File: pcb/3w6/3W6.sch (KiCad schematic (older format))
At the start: 115 parts, among them J1 USB_C Main, J2 USB_C I2C_L, J3 USB_C I2C_R, SW1 SW_Push, SW10 SW_Push, SW11 SW_Push, SW12 SW_Push, SW13 SW_Push, SW14 SW_Push, SW15 SW_Push, SW16 SW_Push, SW17 SW_Push, SW18 SW_Push, SW19 SW_Push, SW2 SW_Push, SW20 SW_Push, SW21 SW_Push, SW22 SW_Push, SW23 SW_Push, SW24 SW_Push, SW25 SW_Push, SW26 SW_Push, SW27 SW_Push, SW28 SW_Push, SW29 SW_Push, SW3 SW_Push, SW30 SW_Push, SW31 SW_Push, SW32 SW_Push, SW33 SW_Push, SW34 SW_Push, SW35 SW_Push, SW36 SW_Push, SW37 SW_Push, SW4 SW_Push, SW5 SW_Push, SW6 SW_Push, SW7 SW_Push, SW8 SW_Push, SW9 SW_Push, U2 TCA9555RTWR, U3 ATmega32U4-MU, Y1 16MHZ

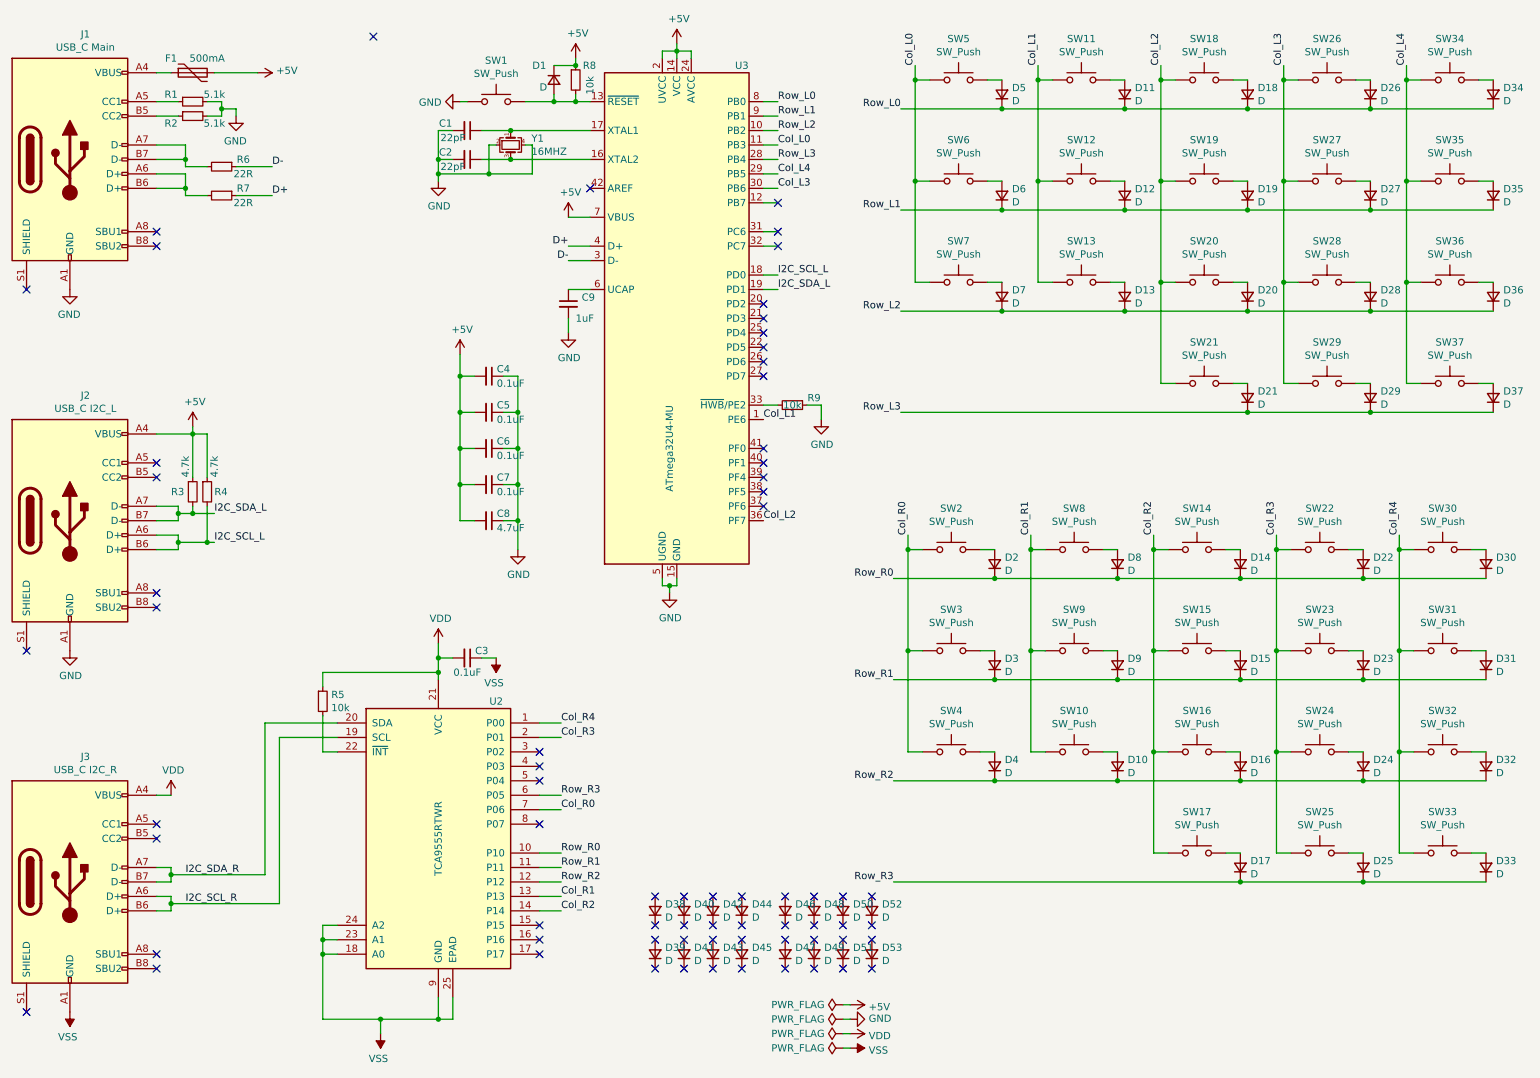
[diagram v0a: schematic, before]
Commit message: add: middle plate chg: rerouting whole board, to eliminate traces under middle plate chg: repositioning components to get a higher clearance in case an aluminium or steel middle plate is used.
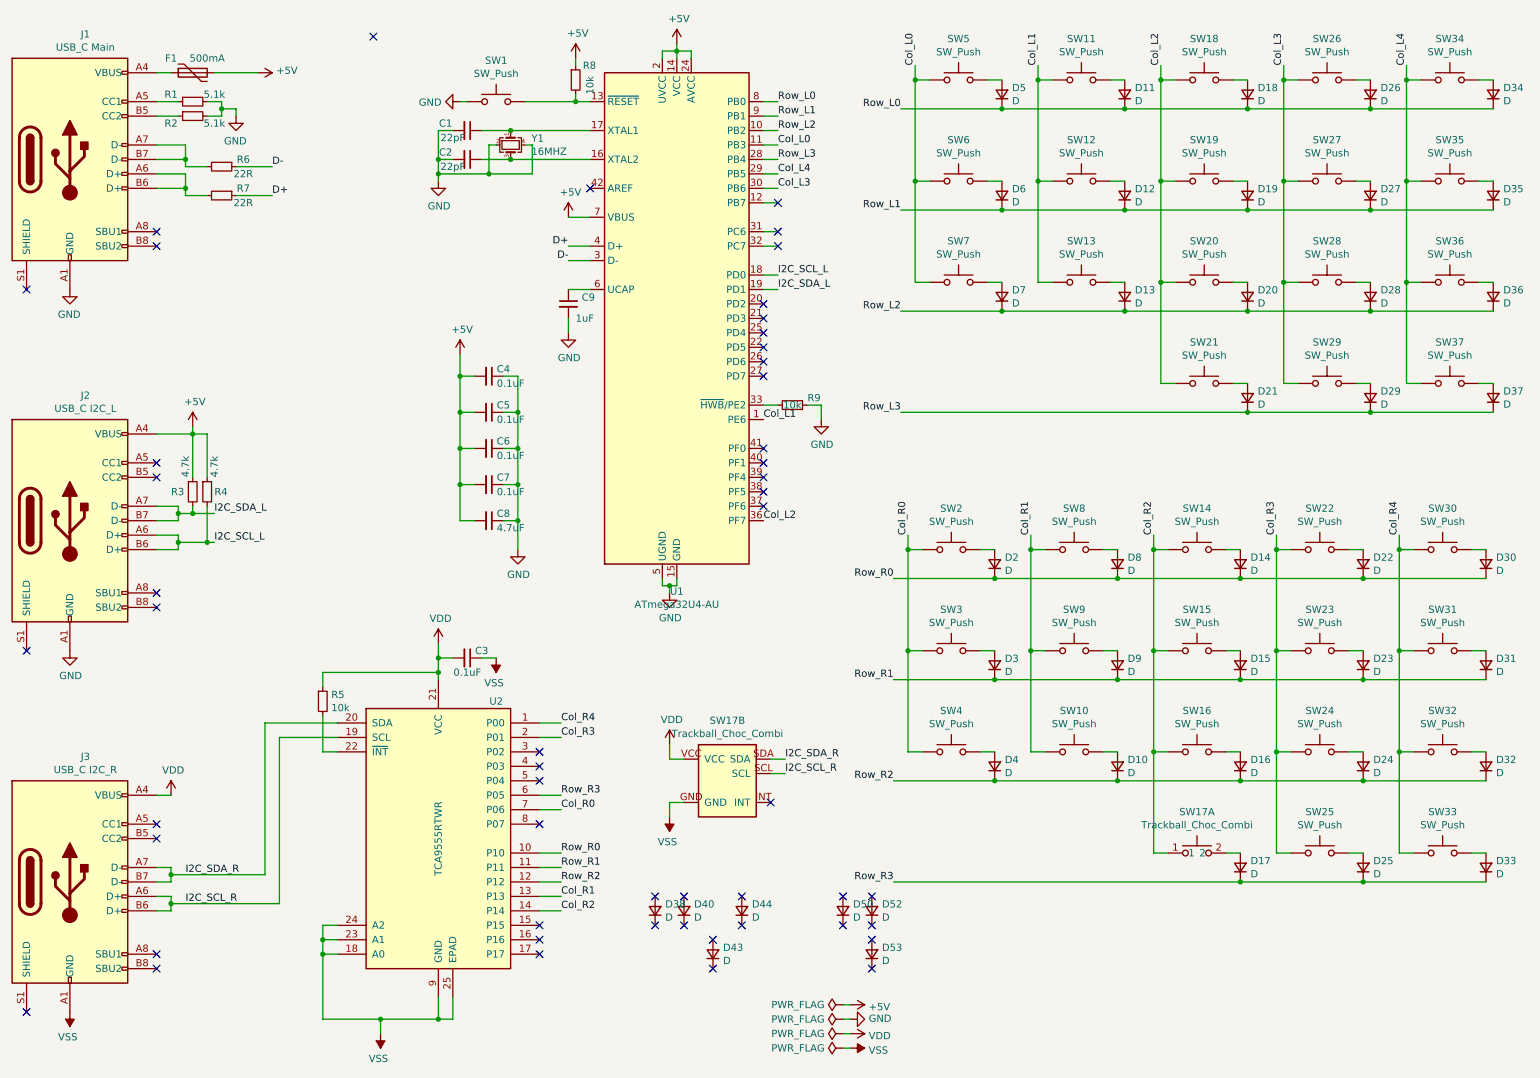
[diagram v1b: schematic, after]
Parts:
- removed D1, D39, D41, D42, D45, D46, D47, D48, D49, D51: D, Weteor:D_SOD-123, symbol Device:D_Small
- removed SW17: SW_Push, Weteor:Kailh_Choc_1u, symbol Switch:SW_Push
- removed U3: ATmega32U4-MU, Package_DFN_QFN:QFN-44-1EP_7x7mm_P0.5mm_EP5.2x5.2mm, symbol MCU_Microchip_ATmega:ATmega32U4-MU
- added SW17: Trackball_Choc_Combi, Weteor:trackball_choc_combi, symbol weteor:Trackball_Choc_Combi
- added U1: ATmega32U4-AU, Package_QFP:TQFP-44_10x10mm_P0.8mm, symbol MCU_Microchip_ATmega:ATmega32U4-AU
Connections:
- net +5V: now also U1.14 (VCC), U1.2 (UVCC), U1.24 (AVCC), U1.34 (VCC), U1.44 (AVCC), U1.7 (VBUS)
- net Col_L0: now also U1.11 (PB3)
- net Col_L1: now also U1.1 (PE6)
- net Col_L2: now also U1.36 (PF7)
- net Col_L3: now also U1.30 (PB6)
- net Col_L4: now also U1.29 (PB5)
- net Col_R2: now also SW17.1
- net D+: now also U1.4 (D+)
- net D-: now also U1.3 (D-)
- net GND: now also U1.15 (GND), U1.23 (GND), U1.35 (GND), U1.43 (GND), U1.5 (UGND)
- net I2C_SCL_L: now also U1.18 (PD0)
- net I2C_SCL_R: now also SW17.SCL
- net I2C_SDA_L: now also U1.19 (PD1)
- net I2C_SDA_R: now also SW17.SDA
- net Row_L0: now also U1.8 (PB0)
- net Row_L1: now also U1.9 (PB1)
- net Row_L2: now also U1.10 (PB2)
- net Row_L3: now also U1.28 (PB4)
- net VDD: now also SW17.VCC
- net VSS: now also SW17.GND
- net at D17.2 (A): now also SW17.2
- net at R8.2, SW1.2: now also U1.13 (~RESET)
- net at C2.1, Y1.3: now also U1.16 (XTAL2)
- net at C1.1, Y1.1: now also U1.17 (XTAL1)
- net at R9.2: now also U1.33 (~HWB~/PE2)
- net at C9.1: now also U1.6 (UCAP)
- no-connect marks 68 -> 51
